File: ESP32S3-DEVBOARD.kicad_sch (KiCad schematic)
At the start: 34 parts, among them J1 G-Switch_GT-USB-7010ASV, J2 PinHeader_1x22_P2.54mm_Vertic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, J3 PinHeader_1x22_P2.54mm_Vertic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, J4 G-Switch_GT-USB-7010ASV, Q1 BC817-40,215, Q2 BC817-40,215, U1 ESP32-S3-WROOM-1, U2 CP2102N-A02-GQFN28R, U3 AMS1117-3.3

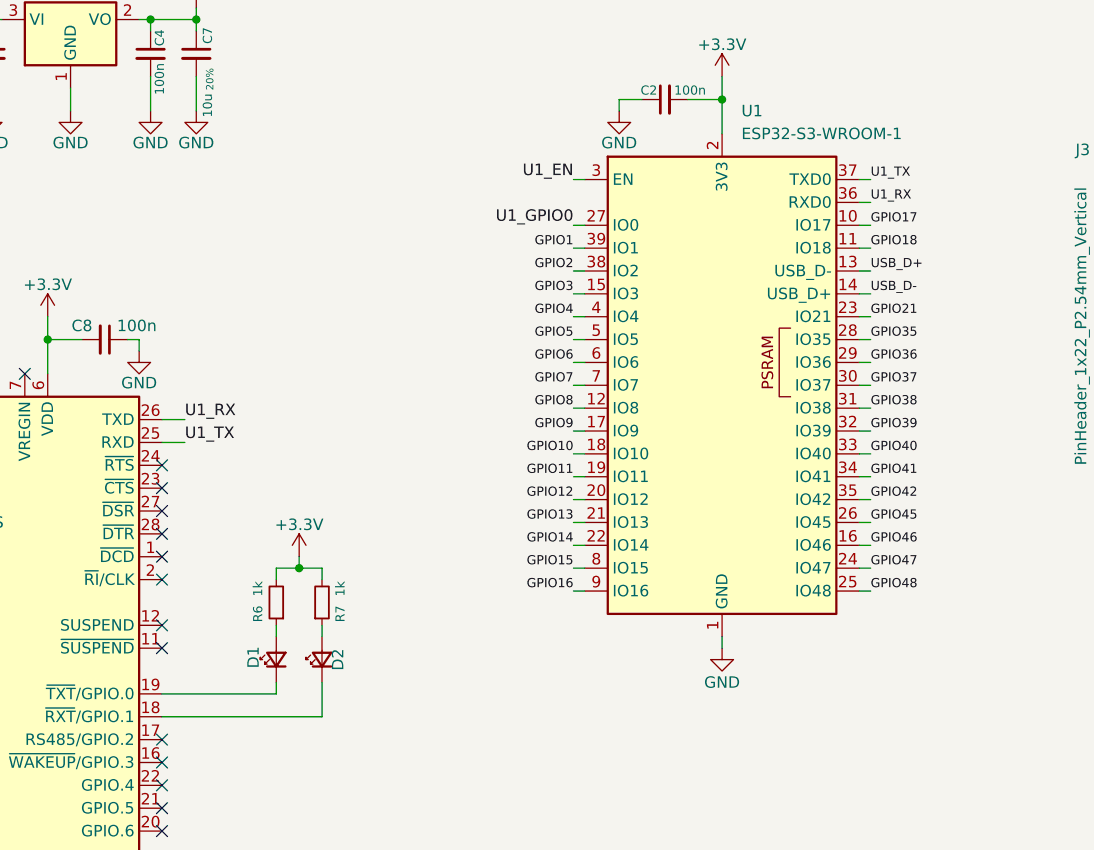
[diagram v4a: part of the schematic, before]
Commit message: Add 1k resistors and leds (red and green 0402)
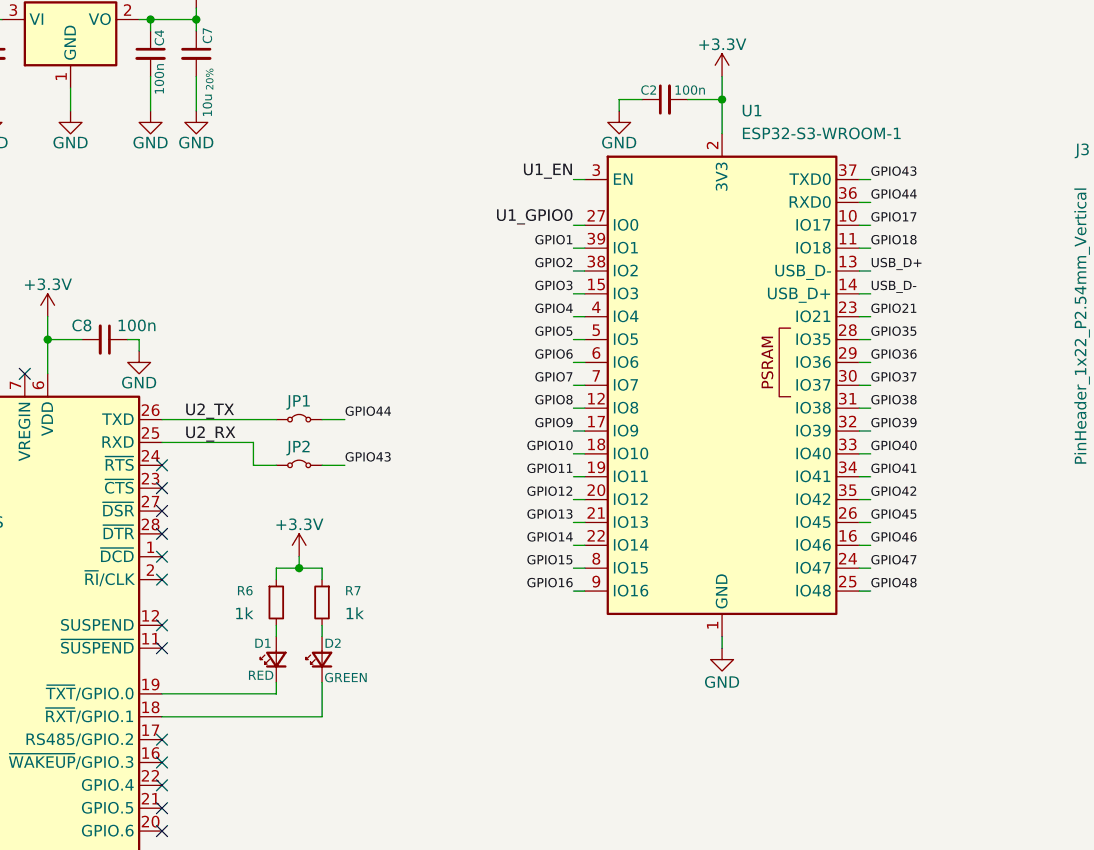
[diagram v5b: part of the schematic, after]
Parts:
- removed D1, D2: LED_Small, symbol Device:LED_Small
- removed R6, R7: 1k, symbol Device:R_Small
- added D1: RED, ESP32S3-DEVBOARD:LED_0402_1005Metric, symbol ESP32S3-DEVBOARD:16-213SDRC/S530-A3/TR8
- added D2: GREEN, ESP32S3-DEVBOARD:LED_0402_1005Metric, symbol ESP32S3-DEVBOARD:16-213/GHC-YR1S1/3T
- added JP1, JP2: Jumper_1x2_P2.54_Bridged, ESP32S3-DEVBOARD:Jumper_1x02_P2.54mm_Bridged, symbol ESP32S3-DEVBOARD:Jumper_1x2_P2.54_Bridged
- added R6, R7: 1k, ESP32S3-DEVBOARD:R_0402_1005Metric, symbol ESP32S3-DEVBOARD:0402WGF1001TCE
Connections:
- net +3.3V: now also R6.1, R7.1
- net GPIO43: now also U1.37 (TXD0), JP2.2 (B)
- net GPIO44: now also U1.36 (RXD0), JP1.2 (B)
- net at U2.18 (~{RXT}/GPIO.1): now also D2.1 (K)
- net at U2.19 (~{TXT}/GPIO.0): now also D1.1 (K)
- net U1_RX renamed U2_TX
- net U2_TX: now also JP1.1 (A); no longer U1.36 (RXD0)
- net U1_TX renamed U2_RX
- net U2_RX: now also JP2.1 (A); no longer U1.37 (TXD0)
- new net: D2.2 (A), R7.2
- new net: D1.2 (A), R6.2

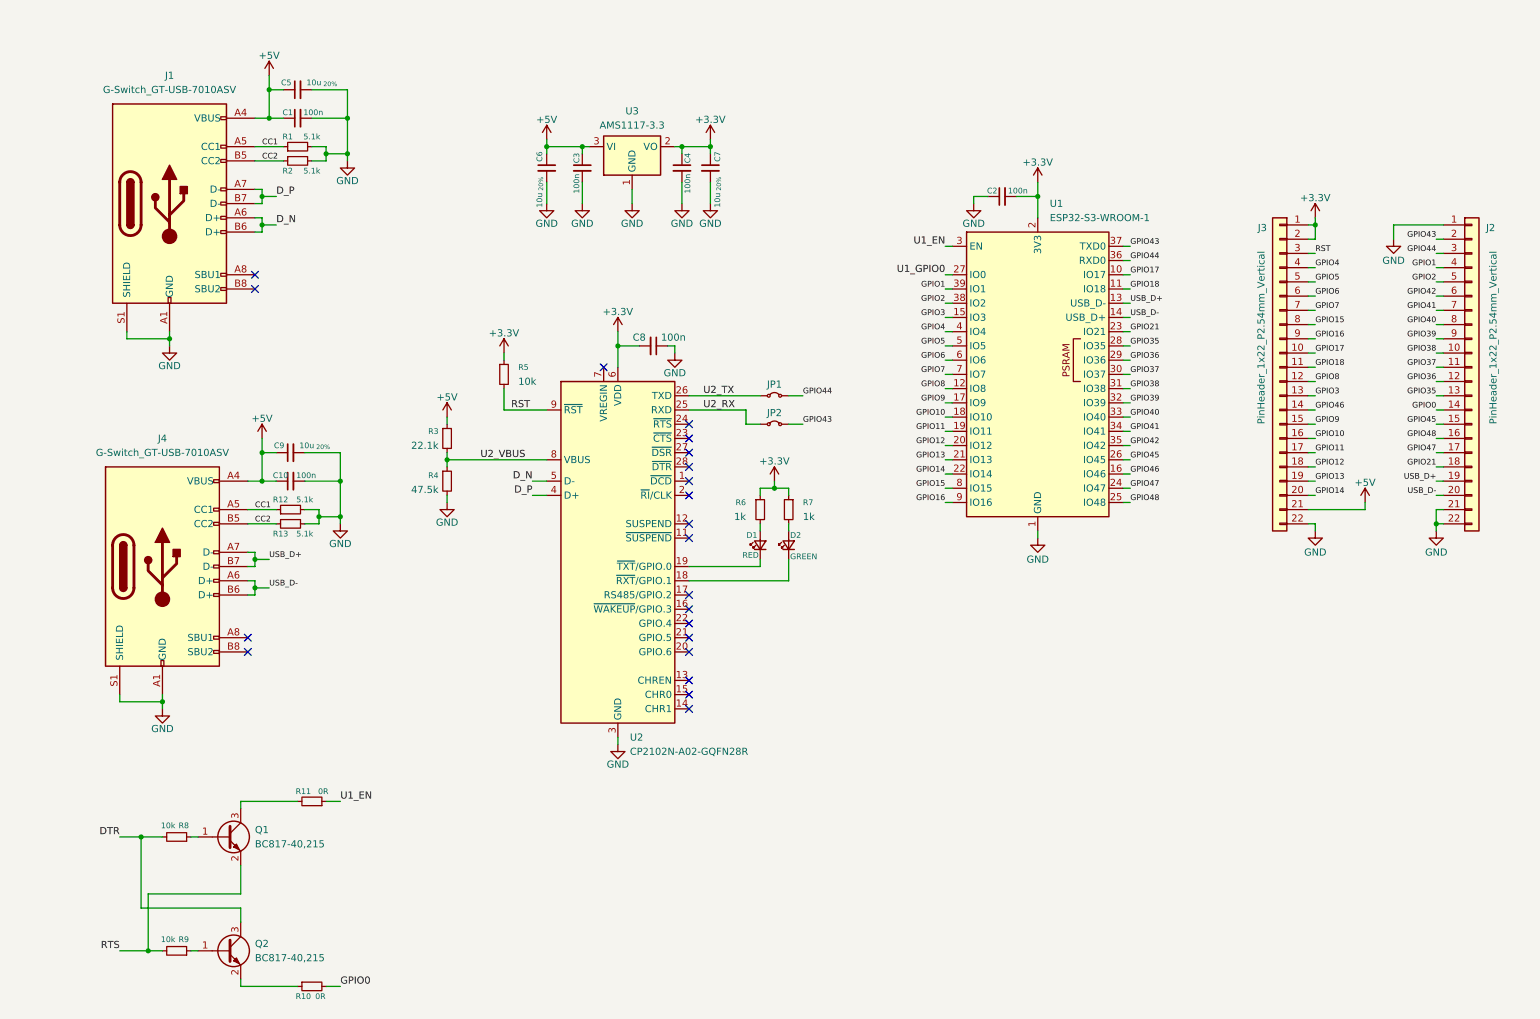
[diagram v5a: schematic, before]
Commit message: Add buttons to lib, 0R resistors and LEDS
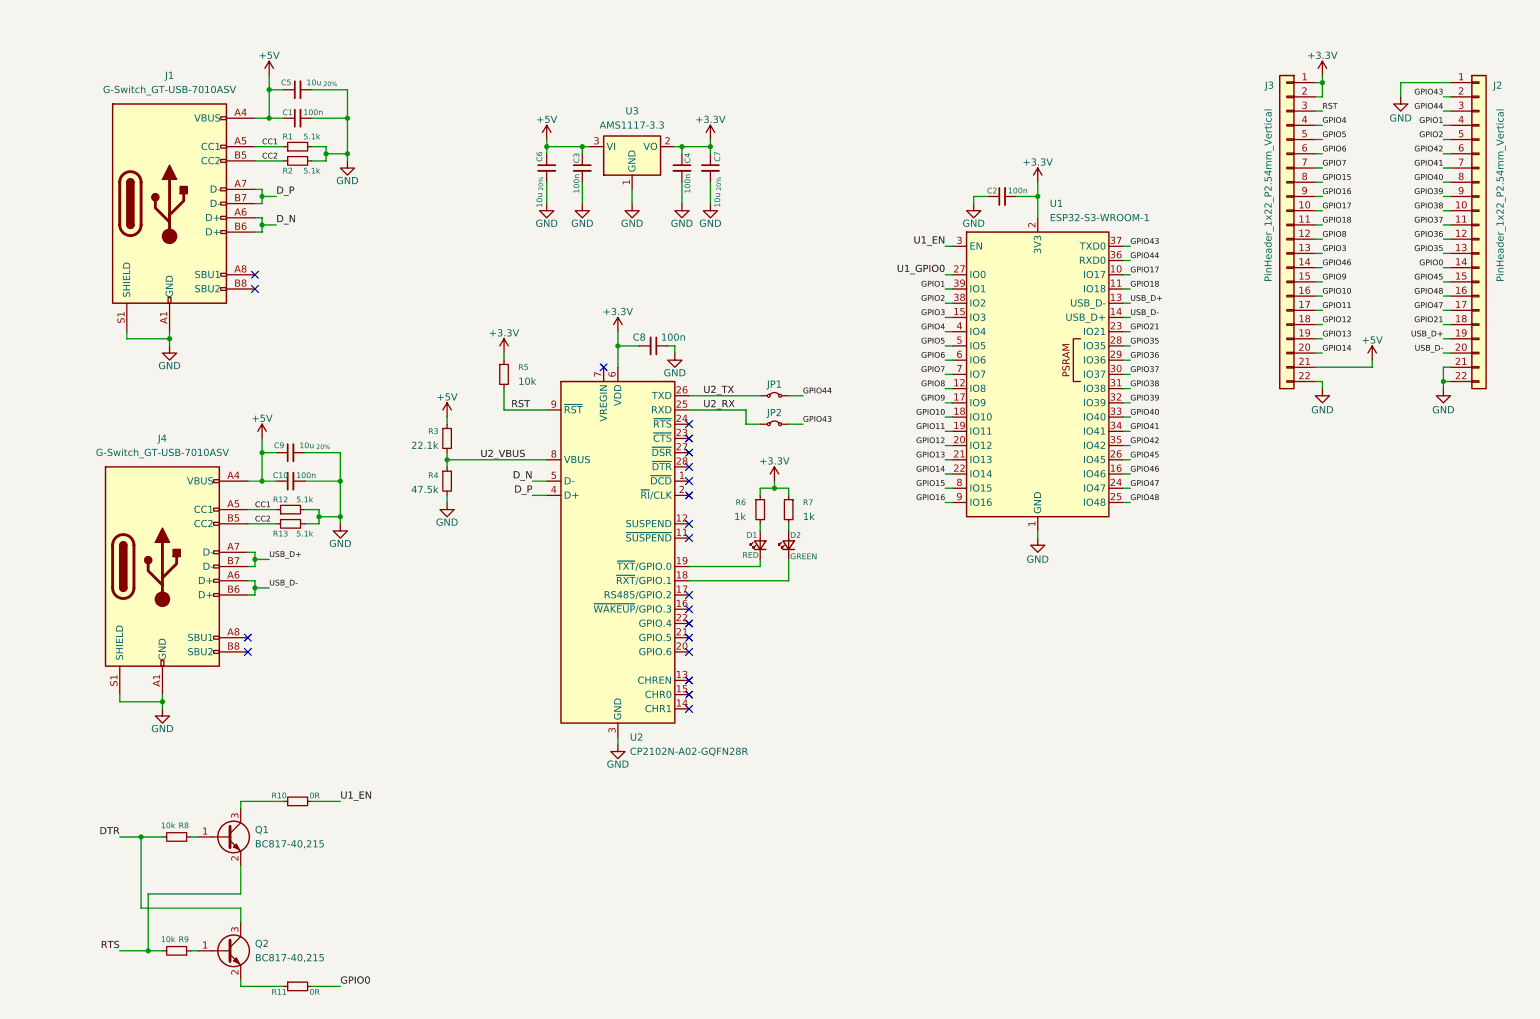
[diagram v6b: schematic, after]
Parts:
- removed R10, R11: 0R, symbol Device:R_Small
- added R10, R11: 0R, ESP32S3-DEVBOARD:R_0402_1005Metric, symbol ESP32S3-DEVBOARD:RC0402FR-070RL
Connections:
- net GPIO0: now also R11.2
- net U1_EN: now also R10.2
- net at Q1.3 (C): now also R10.1
- net at Q2.2 (E): now also R11.1
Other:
- moved on the sheet: J2, J3

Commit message: Add marks, only imu left
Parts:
- added C11, C2, C9: 100n, ESP32S3-DEVBOARD:C_0402_1005Metric, symbol ESP32S3-DEVBOARD:CL05B104KO5NNNC
- added D3: RED, ESP32S3-DEVBOARD:LED_0402_1005Metric, symbol ESP32S3-DEVBOARD:16-213SDRC/S530-A3/TR8
- added D4: GREEN, ESP32S3-DEVBOARD:LED_0402_1005Metric, symbol ESP32S3-DEVBOARD:16-213/GHC-YR1S1/3T
- added R1, R11, R12: 10k, ESP32S3-DEVBOARD:R_0402_1005Metric, symbol ESP32S3-DEVBOARD:RC0402FR-0710KL
- added R13, R14: 1k, ESP32S3-DEVBOARD:R_0402_1005Metric, symbol ESP32S3-DEVBOARD:0402WGF1001TCE
- added SW1, SW2, SW3, SW4: TS-1088-AR02016, ESP32S3-DEVBOARD:TS-1088-AR02016, symbol ESP32S3-DEVBOARD:TS-1088-AR02016
- added U4, U5: USBLC6-2P6, ESP32S3-DEVBOARD:SOT-666, symbol ESP32S3-DEVBOARD:USBLC6-2P6
- renumbered C2 to C1, C8 to C10, C9 to C12, C10 to C13, C5 to C3, C1 to C4, C6 to C5, C3 to C6, C4 to C7, C7 to C8, J3 to J2, J2 to J3, R13 to R10, R10 to R15, R8 to R16, R9 to R17, R11 to R18, R1 to R2, R2 to R3, R5 to R4, R3 to R5, R4 to R6, R6 to R7, R7 to R8, R12 to R9, U3 to U1, U1 to U2, U2 to U3
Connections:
- net U1_GPIO0 is gone; now on net GPIO0: U2.27 (IO0)
- net +3.3V: now also C2.2, R1.1, R11.1, R12.1
- net +5V: now also C11.2, U4.5 (VBUS), U5.5 (VBUS)
- net D_N: now also U4.6 (I/O1); no longer J1.A6 (D+), J1.B6 (D+)
- net D_P: now also U4.4 (I/O2); no longer J1.A7 (D-), J1.B7 (D-)
- net GND: now also C11.1, C2.1, C9.1, D3.1 (K), D4.1 (K), SW1.2, SW2.2, SW3.1, SW4.1, U4.2 (GND), U5.2 (GND)
- net GPIO0: now also SW4.2
- net GPIO13: now also R13.1
- net GPIO14: now also R14.1
- net USB_D+: now also U5.4 (I/O2); no longer J4.A7 (D-), J4.B7 (D-)
- net USB_D-: now also U5.6 (I/O1); no longer J4.A6 (D+), J4.B6 (D+)
- net U1_EN renamed EN
- net EN: now also C9.2, R1.2, SW3.2
- new net: R12.2, SW2.1
- new net: R11.2, SW1.1
- new net: J4.A6 (D+), J4.B6 (D+), U5.3 (I/O2)
- new net: J4.A7 (D-), J4.B7 (D-), U5.1 (I/O1)
- new net: J1.A7 (D-), J1.B7 (D-), U4.1 (I/O1)
- new net: J1.A6 (D+), J1.B6 (D+), U4.3 (I/O2)
- new net: D4.2 (A), R14.2
- new net: D3.2 (A), R13.2
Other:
- note added: "USB for OTG (ESP)"
- note added: "USB for TTL"
- moved on the sheet: C1, C10, C12, C13, C3, C4, C5, C6, C7, C8, D1, D2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

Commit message: Finnished a schematic. Rev 1.0.0
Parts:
- removed R11, R12: 10k, ESP32S3-DEVBOARD:R_0402_1005Metric, symbol ESP32S3-DEVBOARD:RC0402FR-0710KL
- added C12, C13: 100n, ESP32S3-DEVBOARD:C_0402_1005Metric, symbol ESP32S3-DEVBOARD:CL05B104KO5NNNC
- added JP3, JP4, JP5, JP6, JP7: Jumper_1x2_P2.54_Bridged, ESP32S3-DEVBOARD:Jumper_1x02_P2.54mm_Bridged, symbol ESP32S3-DEVBOARD:Jumper_1x2_P2.54_Bridged
- added R13, R14, R15: 10k, ESP32S3-DEVBOARD:R_0402_1005Metric, symbol ESP32S3-DEVBOARD:RC0402FR-0710KL
- added U5: BMI270, ESP32S3-DEVBOARD:BMI270, symbol ESP32S3-DEVBOARD:BMI270
- renumbered C2 to C1, C11 to C10, C10 to C11, C12 to C14, C13 to C15, C1 to C2, C5 to C3, C6 to C4, C7 to C5, C8 to C6, C9 to C7, C3 to C8, C4 to C9, J2 to J1, J3 to J2, J1 to J3, R15 to R1, R6 to R10, R7 to R11, R8 to R12, R9 to R16, R10 to R17, R16 to R2, R13 to R20, R14 to R21, R1 to R3, R17 to R4, R18 to R5, R2 to R6, R3 to R7, R4 to R8, R5 to R9, SW3 to SW1, SW4 to SW2, SW1 to SW3, SW2 to SW4, U4 to U3, U3 to U4, U5 to U6
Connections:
- net +3.3V: now also C12.1, C13.1, JP5.1 (A), R13.1, R14.1, U5.12 (CSB), U5.5 (VDDIO), U5.8 (VDD)
- net GND: now also C12.2, C13.2, R15.2, U5.6 (GNDIO), U5.7 (GND)
- net GPIO15: now also SW3.1
- net GPIO16: now also SW4.1
- net GPIO4: now also JP3.1 (A)
- net GPIO5: now also JP4.1 (A)
- net GPIO6: now also JP7.1 (A)
- net GPIO7: now also JP6.1 (A)
- new net: JP5.2 (B), R15.1
- new net INT1: JP6.2 (B), U5.4 (INT1)
- new net INT2: JP7.2 (B), U5.9 (INT2)
- new net I^{2}C_SCL: JP3.2 (B), R14.2, U5.13 (SCX)
- new net I^{2}C_SDA: JP4.2 (B), R13.2, U5.14 (SDX)
- no-connect marks 21 -> 26
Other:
- company: (none) -> FALCON
- title: (none) -> ESP32-S3-WROOM1 Devboard
- moved on the sheet: C2, C7, R3, SW3, SW4, U2
